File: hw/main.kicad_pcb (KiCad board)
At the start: 2 copper layers, 90 parts, among them J1 UART_01X03, J2 SWD_01X04, J3 SWD_01X04, J4 IDC_02X07, J5 IDC_02X07, J8 SMA, SW1 LCD_BTN, U1 STM32F405RGTx, U10 MCP1826S, U11 MCP1826S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

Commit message: placement component to pcb
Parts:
- removed U12: OSRB38C9BA, KLIB_Opto:OSRB8C9BA
- added C36: 100n, Capacitor_SMD:C_0805_2012Metric, F.Cu at (167.0, 100.3)
- added C37: 1u/50V, Capacitor_SMD:C_0805_2012Metric, F.Cu at (167.0, 98.4)
- added D2: LTST-G563ZEGBW, KLIB_Opto:LED_RGB_5050-6, F.Cu at (140.0, 60.0)
- added D3: LTST-G563ZEGBW, KLIB_Opto:LED_RGB_5050-6, F.Cu at (95.0, 80.0)
- added D4: LTST-G563ZEGBW, KLIB_Opto:LED_RGB_5050-6, F.Cu at (140.0, 100.0)
- added D5: LTST-G563ZEGBW, KLIB_Opto:LED_RGB_5050-6, F.Cu at (185.0, 80.0)
- added H1: M3, KLIB_Mechanical:Bolt_M3, F.Cu at (90.0, 40.0)
- added H2: M3, KLIB_Mechanical:Bolt_M3, F.Cu at (190.0, 40.0)
- added H3: M3, KLIB_Mechanical:Bolt_M3, F.Cu at (190.0, 115.0)
- added H4: M3, KLIB_Mechanical:Bolt_M3, F.Cu at (90.0, 115.0)
- added J6: IDC_02X03, Connector_IDC:IDC-Header_2x03_P2.54mm_Vertical, F.Cu at (137.5, 41.0)
- added J7: IDC_02X13, Connector_IDC:IDC-Header_2x13_P2.54mm_Vertical, F.Cu at (91.8, 51.0)
- added J9: IDC_02X05, Connector_IDC:IDC-Header_2x05_P2.54mm_Vertical, F.Cu at (91.0, 101.1)
- U11: value MCP1826S -> OSRB38C9BA; footprint Package_TO_SOT_SMD:SOT-223-3_TabPin2 -> KLIB_Opto:OSRB8C9BA_Horizontal
- U6: value AD8542 -> STM32F405RGTx; footprint Package_SO:SOIJ-8_5.3x5.3mm_P1.27mm -> Package_QFP:TQFP-64_10x10mm_P0.5mm
- U7: value STM32F405RGTx -> HM-TRP-869S; footprint Package_QFP:TQFP-64_10x10mm_P0.5mm -> KLIB_RF_Module:HM-TRP-SMD
- U8: value HM-TRP-869S -> ULN2003; footprint KLIB_RF_Module:HM-TRP-SMD -> Package_SO:SOIC-16_3.9x9.9mm_P1.27mm
- U9: value ULN2003 -> MCP1826S; footprint Package_SO:SOIC-16_3.9x9.9mm_P1.27mm -> Package_TO_SOT_SMD:SOT-223-3_TabPin2
- moved C26 121.4 mm to (92.0, 108.2), turned to 180 degrees
- moved C4 119.1 mm to (100.0, 107.2), turned to 180 degrees
- moved C6 112.9 mm to (105.8, 94.0), turned to 90 degrees
- moved SW1 109.2 mm to (96.0, 113.0), turned to 270 degrees
- moved J5 109.0 mm to (165.4, 41.0), turned to 90 degrees
- moved C29 107.7 mm to (92.2, 71.8)
- moved C28 107.6 mm to (92.2, 61.6)
- moved C8 104.1 mm to (103.2, 111.2), turned to 180 degrees
- moved C27 103.5 mm to (92.2, 59.7)
- moved J2 101.7 mm to (97.0, 95.1), turned to 180 degrees
- moved C32 100.0 mm to (103.0, 61.6)
- moved C7 99.3 mm to (118.8, 106.0)
- moved J1 95.5 mm to (125.5, 116.8), turned to 270 degrees
- moved C34 95.5 mm to (103.0, 59.7)
- moved R20 95.3 mm to (101.0, 78.0)
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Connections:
- U1 pad 10: /Address/A6 -> /Address/A1
- U1 pad 11: /Address/A7 -> /Address/A0
- U1 pad 3: /Address/A0 -> /Address/A7
- U1 pad 4: /Address/A1 -> /Address/A6
- U1 pad 5: /Address/A2 -> /Address/A5
- U1 pad 6: /Address/A3 -> /Address/A4
- U1 pad 8: /Address/A4 -> /Address/A3
- U1 pad 9: /Address/A5 -> /Address/A2
- U10 pad 1: +5V5 -> +5V
- U10 pad 3: +5V -> +3V3
- U11 pad 1: +5V -> /Back/IR_RX
- U11 pad 3: +3V3 -> Net-(C35-Pad1)
- U3 pad 5: Net-(C13-Pad1) -> Net-(C11-Pad1)
- U3 pad 6: Net-(C15-Pad2) -> Net-(C12-Pad2)
- U3 pad 7: Net-(C15-Pad2) -> Net-(C12-Pad2)
- U5 pad 1: Net-(C12-Pad2) -> Net-(C15-Pad2)
- U5 pad 2: Net-(C12-Pad2) -> Net-(C15-Pad2)
- U5 pad 3: Net-(C11-Pad1) -> Net-(C13-Pad1)
- U5 pad 5: (no net) -> Net-(C15-Pad2)
- U5 pad 6: (no net) -> Net-(C17-Pad2)
- U5 pad 7: (no net) -> Net-(C17-Pad2)
- U6 pad 1: Net-(C17-Pad2) -> +3V3
- U6 pad 2: Net-(C17-Pad2) -> Net-(U6-Pad2)
- U6 pad 3: Net-(C15-Pad2) -> Net-(U6-Pad3)
- U6 pad 4: (no net) -> Net-(U6-Pad4)
- U6 pad 5: (no net) -> Net-(U6-Pad5)
- U6 pad 6: (no net) -> Net-(U6-Pad6)
- U6 pad 7: (no net) -> /Sound/Sound MCU/~RST
- U6 pad 8: (no net) -> Net-(U6-Pad8)
- U7 pad 2: Net-(U7-Pad2) -> /Main MCU/RF_UART_RX
- U7 pad 3: Net-(U7-Pad3) -> GND
- U7 pad 4: Net-(U7-Pad4) -> /RF/RF_UART_RX
- U7 pad 5: Net-(U7-Pad5) -> /Main MCU/~RF_CONFIG
- U7 pad 6: Net-(U7-Pad6) -> /Main MCU/~RF_ENABLE
- U7 pad 7: /Sound/Sound MCU/~RST -> Net-(U7-Pad7)
- U7 pad 8: Net-(U7-Pad8) -> GND
- U7 pad 9: Net-(U7-Pad9) -> Net-(D1-Pad1)
- U8 pad 1: +3V3 -> /LED/PWM_R
- U8 pad 2: /Main MCU/RF_UART_RX -> /LED/PWM_R
- U8 pad 3: GND -> /LED/PWM_G
- U8 pad 4: /RF/RF_UART_RX -> /LED/PWM_G
- U8 pad 5: /Main MCU/~RF_CONFIG -> /LED/PWM_B
- U8 pad 6: /Main MCU/~RF_ENABLE -> /LED/PWM_B
- U8 pad 7: Net-(U8-Pad7) -> /LED/PWM_B
- U8 pad 9: Net-(D1-Pad1) -> +5V
- U9 pad 1: /LED/PWM_R -> +5V5
- U9 pad 2: /LED/PWM_R -> GND
- U9 pad 3: /LED/PWM_G -> +5V
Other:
- board outline added: 110 x 85 mm

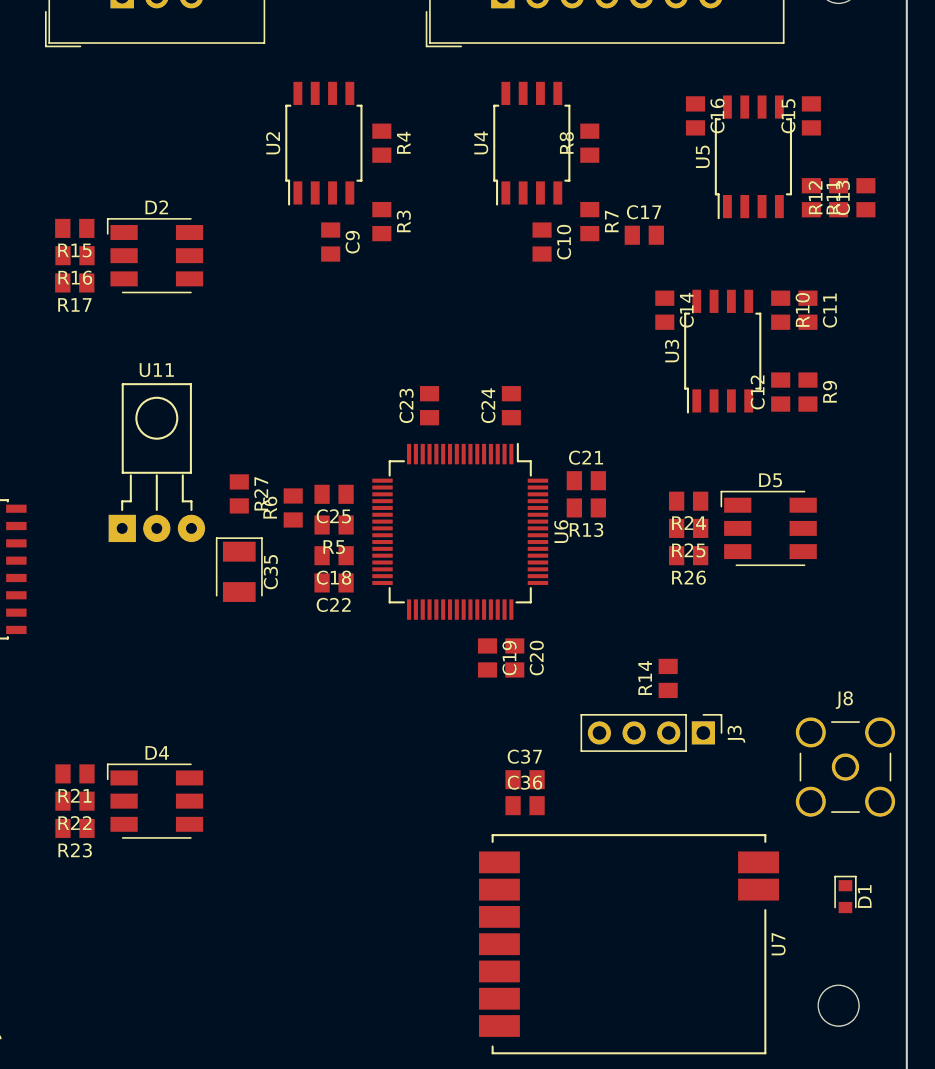
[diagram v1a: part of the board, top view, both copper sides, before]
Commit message: updated schematic added buffer to gun uart and updated pcb
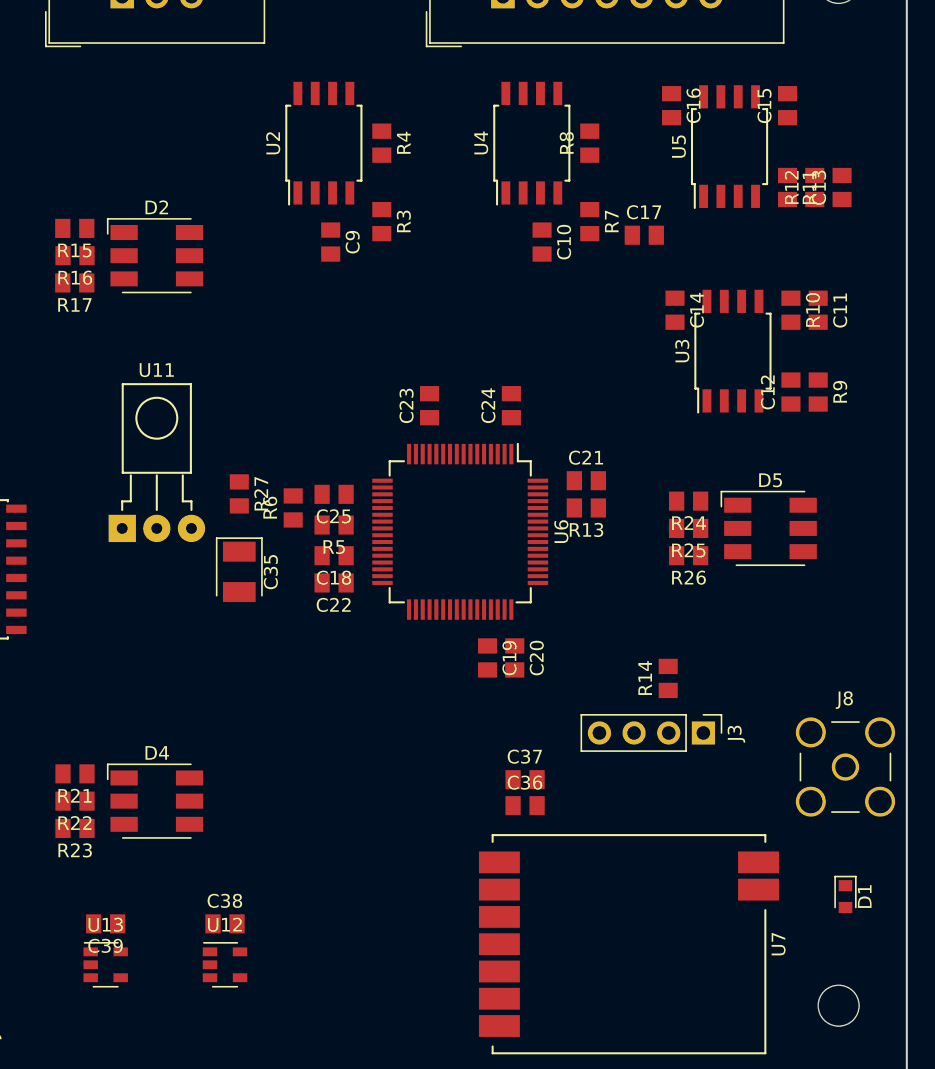
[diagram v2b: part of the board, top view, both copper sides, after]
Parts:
- added C38: 100n, Capacitor_SMD:C_0805_2012Metric, F.Cu at (145.0, 109.0)
- added C39: 100n, Capacitor_SMD:C_0805_2012Metric, F.Cu at (136.2, 109.0)
- added U12: 74AHC1G08, Package_TO_SOT_SMD:SOT-23-5, F.Cu at (145.0, 112.0)
- added U13: 74AHC1G08, Package_TO_SOT_SMD:SOT-23-5, F.Cu at (136.2, 112.0)
- moved C13 1.90 mm to (190.2, 55.0)
- moved C15 1.90 mm to (186.2, 49.0)
- moved C16 1.90 mm to (177.8, 49.0)
- moved R11 1.90 mm to (186.2, 55.0)
- moved R12 1.90 mm to (188.2, 55.0)
- moved U5 1.90 mm to (182.0, 52.0)
- moved C11 0.75 mm to (188.5, 64.0)
- moved C12 0.75 mm to (186.5, 70.0)
- moved C14 0.75 mm to (178.0, 64.0)
- moved R10 0.75 mm to (186.5, 64.0)
- moved R9 0.75 mm to (188.5, 70.0)
- moved U3 0.75 mm to (182.2, 67.0)
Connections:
- J9 pad 5: /Gun/GUN_UART_RX -> /Gun/GUN_RX
- J9 pad 6: /Gun/GUN_UART_RX -> /Gun/GUN_RX
- J9 pad 7: /Main MCU/GUN_UART_RX -> /Gun/GUN_TX
- J9 pad 8: /Main MCU/GUN_UART_RX -> /Gun/GUN_TX

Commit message: updated pcb placement
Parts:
- moved J7 12.3 mm to (99.0, 41.0)
- moved J4 10.0 mm to (99.0, 51.0)
- moved J6 7.54 mm to (145.0, 41.0)
- moved U8 6.00 mm to (121.0, 83.0), turned to 90 degrees
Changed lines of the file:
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@@
   )
   (module Connector_IDC:IDC-Header_2x03_P2.54mm_Vertical (layer F.Cu)
-    (at 137.46 41 90)
+    (at 145 41 90)
     (descr "Through hole straight IDC box header, 2x03, 2.54mm pitch, double rows")
     (tags "Through hole IDC box header THT 2x03 2.54mm double row")
@@
   )
   (module Connector_IDC:IDC-Header_2x07_P2.54mm_Vertical (layer F.Cu)
-    (at 99.38 41 90)
+    (at 99 51 90)
     (descr "Through hole straight IDC box header, 2x07, 2.54mm pitch, double rows")
     (tags "Through hole IDC box header THT 2x07 2.54mm double row")
@@
   )
   (module Connector_IDC:IDC-Header_2x13_P2.54mm_Vertical (layer F.Cu)
-    (at 91.76 51 90)
+    (at 99 41 90)
     (descr "Through hole straight IDC box header, 2x13, 2.54mm pitch, double rows")
     (tags "Through hole IDC box header THT 2x13 2.54mm double row")
@@
   )
   (module Package_SO:SOIC-16_3.9x9.9mm_P1.27mm (layer F.Cu)
-    (at 127 83)
+    (at 121 83 90)
     (descr "16-Lead Plastic Small Outline (SL) - Narrow, 3.90 mm Body [SOIC] (see Microchip Packaging Specification 00000049BS.pdf)")
     (tags "SOIC 1.27")
     (attr smd)
-    (fp_text reference U8 (at 0 -6) (layer F.SilkS)
-      (effects (font (size 1 1) (thickness 0.15)))
-    )
-    (fp_text value ULN2003 (at 0 6) (layer F.Fab)
-      (effects (font (size 1 1) (thickness 0.15)))
-    )
-    (fp_text user %R (at 0 0) (layer F.Fab)
+    (fp_text reference U8 (at 0 -6 90) (layer F.SilkS)
+      (effects (font (size 1 1) (thickness 0.15)))
+    )
+    (fp_text value ULN2003 (at 0 6 90) (layer F.Fab)
+      (effects (font (size 1 1) (thickness 0.15)))
+    )
+    (fp_text user %R (at 0 0 90) (layer F.Fab)
       (effects (font (size 0.9 0.9) (thickness 0.135)))
     )
@@
     (fp_line (start -2.075 5.075) (end 2.075 5.075) (layer F.SilkS) (width 0.15))
     (fp_line (start -2.075 -5.05) (end -3.45 -5.05) (layer F.SilkS) (width 0.15))
-    (pad 1 smd rect (at -2.7 -4.445) (size 1.5 0.6) (layers F.Cu F.Paste F.Mask)
+    (pad 1 smd rect (at -2.7 -4.445 90) (size 1.5 0.6) (layers F.Cu F.Paste F.Mask)
       (net 53 /LED/PWM_R))
-    (pad 2 smd rect (at -2.7 -3.175) (size 1.5 0.6) (layers F.Cu F.Paste F.Mask)
+    (pad 2 smd rect (at -2.7 -3.175 90) (size 1.5 0.6) (layers F.Cu F.Paste F.Mask)
       (net 53 /LED/PWM_R))
-    (pad 3 smd rect (at -2.7 -1.905) (size 1.5 0.6) (layers F.Cu F.Paste F.Mask)
+    (pad 3 smd rect (at -2.7 -1.905 90) (size 1.5 0.6) (layers F.Cu F.Paste F.Mask)
       (net 54 /LED/PWM_G))
-    (pad 4 smd rect (at -2.7 -0.635) (size 1.5 0.6) (layers F.Cu F.Paste F.Mask)
+    (pad 4 smd rect (at -2.7 -0.635 90) (size 1.5 0.6) (layers F.Cu F.Paste F.Mask)
       (net 54 /LED/PWM_G))
-    (pad 5 smd rect (at -2.7 0.635) (size 1.5 0.6) (layers F.Cu F.Paste F.Mask)
+    (pad 5 smd rect (at -2.7 0.635 90) (size 1.5 0.6) (layers F.Cu F.Paste F.Mask)
       (net 55 /LED/PWM_B))
-    (pad 6 smd rect (at -2.7 1.905) (size 1.5 0.6) (layers F.Cu F.Paste F.Mask)
+    (pad 6 smd rect (at -2.7 1.905 90) (size 1.5 0.6) (layers F.Cu F.Paste F.Mask)
       (net 55 /LED/PWM_B))
-    (pad 7 smd rect (at -2.7 3.175) (size 1.5 0.6) (layers F.Cu F.Paste F.Mask)
+    (pad 7 smd rect (at -2.7 3.175 90) (size 1.5 0.6) (layers F.Cu F.Paste F.Mask)
       (net 55 /LED/PWM_B))
-    (pad 8 smd rect (at -2.7 4.445) (size 1.5 0.6) (layers F.Cu F.Paste F.Mask)
-      (net 2 GND))
-    (pad 9 smd rect (at 2.7 4.445) (size 1.5 0.6) (layers F.Cu F.Paste F.Mask)
-      (net 13 +5V))
-    (pad 10 smd rect (at 2.7 3.175) (size 1.5 0.6) (layers F.Cu F.Paste F.Mask)
+    (pad 8 smd rect (at -2.7 4.445 90) (size 1.5 0.6) (layers F.Cu F.Paste F.Mask)
+      (net 2 GND))
+    (pad 9 smd rect (at 2.7 4.445 90) (size 1.5 0.6) (layers F.Cu F.Paste F.Mask)
+      (net 13 +5V))
+    (pad 10 smd rect (at 2.7 3.175 90) (size 1.5 0.6) (layers F.Cu F.Paste F.Mask)
       (net 15 /Back/LED_PWM_B))
-    (pad 11 smd rect (at 2.7 1.905) (size 1.5 0.6) (layers F.Cu F.Paste F.Mask)
+    (pad 11 smd rect (at 2.7 1.905 90) (size 1.5 0.6) (layers F.Cu F.Paste F.Mask)
       (net 15 /Back/LED_PWM_B))
-    (pad 12 smd rect (at 2.7 0.635) (size 1.5 0.6) (layers F.Cu F.Paste F.Mask)
+    (pad 12 smd rect (at 2.7 0.635 90) (size 1.5 0.6) (layers F.Cu F.Paste F.Mask)
       (net 15 /Back/LED_PWM_B))
-    (pad 13 smd rect (at 2.7 -0.635) (size 1.5 0.6) (layers F.Cu F.Paste F.Mask)
+    (pad 13 smd rect (at 2.7 -0.635 90) (size 1.5 0.6) (layers F.Cu F.Paste F.Mask)
       (net 24 /Back/LED_PWM_G))
-    (pad 14 smd rect (at 2.7 -1.905) (size 1.5 0.6) (layers F.Cu F.Paste F.Mask)
+    (pad 14 smd rect (at 2.7 -1.905 90) (size 1.5 0.6) (layers F.Cu F.Paste F.Mask)
       (net 24 /Back/LED_PWM_G))
-    (pad 15 smd rect (at 2.7 -3.175) (size 1.5 0.6) (layers F.Cu F.Paste F.Mask)
+    (pad 15 smd rect (at 2.7 -3.175 90) (size 1.5 0.6) (layers F.Cu F.Paste F.Mask)
       (net 11 /Back/LED_PWM_R))
-    (pad 16 smd rect (at 2.7 -4.445) (size 1.5 0.6) (layers F.Cu F.Paste F.Mask)
+    (pad 16 smd rect (at 2.7 -4.445 90) (size 1.5 0.6) (layers F.Cu F.Paste F.Mask)
       (net 11 /Back/LED_PWM_R))
     (model ${KISYS3DMOD}/Package_SO.3dshapes/SOIC-16_3.9x9.9mm_P1.27mm.wrl

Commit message: updated pcb
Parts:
- moved C38 12.1 mm to (133.0, 107.2)
- moved U12 12.1 mm to (133.0, 110.2), turned to 90 degrees
- moved C39 9.66 mm to (126.8, 107.2), turned to 0 degrees
- moved U13 9.66 mm to (126.8, 110.2), turned to 90 degrees
- moved C26 8.46 mm to (99.0, 113.0), turned to 270 degrees
- moved R6 4.24 mm to (153.0, 75.5), turned to 0 degrees
- moved C19 4.03 mm to (168.2, 90.0), turned to 0 degrees
- moved C20 2.50 mm to (168.2, 88.0), turned to 0 degrees
- moved D1 1.80 mm to (191.5, 105.5), turned to 315 degrees
- moved C5 0.50 mm to (113.9, 112.0)
- moved U7 0.38 mm to (174.2, 110.5)
- moved R5 0.25 mm to (153.0, 79.5)
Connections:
- U1 pad 22: /LED/PWM_R -> /LED/PWM_B
- U1 pad 26: /LED/PWM_B -> /LED/PWM_R
- U6 pad 14: /Main MCU/SOUND_SEL0 -> Net-(U6-Pad14)
- U6 pad 15: /Main MCU/SOUND_SEL1 -> Net-(U6-Pad15)
- U6 pad 44: Net-(U6-Pad44) -> /Main MCU/SOUND_SEL0
- U6 pad 45: Net-(U6-Pad45) -> /Main MCU/SOUND_SEL1
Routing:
- net /Main MCU/SOUND_SEL1: track 0.00 -> 62.5 mm, vias 0 -> 2
- net /Main MCU/SOUND_SEL0: track 0.00 -> 61.7 mm, vias 0 -> 2
- net /Sound/SOUND_UART_RX: track 0.00 -> 60.8 mm, vias 0 -> 2
- net /Main MCU/SOUND_UART_RX: track 0.00 -> 60.3 mm, vias 0 -> 2
- net +3V3: track 0.00 -> 35.8 mm
- net /LED/PWM_R: track 0.00 -> 29.6 mm
- net /LED/PWM_B: track 0.00 -> 28.6 mm
- net /LED/PWM_G: track 0.00 -> 28.5 mm
- net /Main MCU/SWDIO: track 0.00 -> 23.3 mm
- net /Gun/GUN_UART_RX: track 0.00 -> 23.1 mm
- net /Main MCU/GUN_UART_RX: track 0.00 -> 22.2 mm
- net +5V5: track 0.00 -> 17.8 mm
- net /Main MCU/SWDCLK: track 0.00 -> 17.7 mm
- net /Display/~BTN: track 0.00 -> 16.9 mm
- net /Main MCU/DEBUG_UART_RX: track 0.00 -> 15.0 mm
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- added copper zone on B.Cu, net GND
- added copper zone on F.Cu, net GND

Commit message: updated pcb
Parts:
- moved C2 4.28 mm to (103.5, 93.5), turned to 180 degrees
- moved C6 2.70 mm to (103.5, 95.5), turned to 180 degrees
- moved R2 2.30 mm to (99.8, 90.8), turned to 270 degrees
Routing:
- net /Main MCU/~RF_CONFIG: track 0.00 -> 73.5 mm, vias 0 -> 2
- net /Main MCU/~RF_ENABLE: track 0.00 -> 71.0 mm, vias 0 -> 2
- net /Main MCU/RF_UART_RX: track 0.00 -> 69.2 mm, vias 0 -> 2
- net /RF/RF_UART_RX: track 0.00 -> 65.5 mm, vias 0 -> 2
- net /Main MCU/SWDIO: track 23.3 -> 16.9 mm
- net Net-(C2-Pad1): track 3.77 -> 5.33 mm

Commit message: updated pcb
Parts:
- moved C34 19.6 mm to (122.0, 64.8), turned to 90 degrees
- moved C33 18.4 mm to (120.0, 64.8), turned to 90 degrees
- moved C30 14.8 mm to (104.0, 64.8), turned to 90 degrees
- moved U10 12.1 mm to (115.2, 64.8), turned to 90 degrees
- moved C29 12.0 mm to (102.0, 64.8), turned to 90 degrees
- moved C31 10.5 mm to (108.5, 64.8), turned to 90 degrees
- moved C32 8.11 mm to (110.5, 64.8), turned to 90 degrees
- moved U9 5.37 mm to (97.2, 64.8), turned to 90 degrees
- moved C27 5.35 mm to (90.5, 64.8), turned to 90 degrees
- moved C28 3.17 mm to (92.5, 64.8), turned to 90 degrees
- moved R14 2.00 mm to (177.5, 89.0), turned to 270 degrees
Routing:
- net +5V5: track 17.8 -> 110.9 mm
- net /Sound/Sound MCU/~RST: track 0.00 -> 37.1 mm, vias 0 -> 1
- net +5V: track 10.2 -> 32.7 mm
- net /Sound/Sound MCU/SWDCLK: track 0.00 -> 15.4 mm
- net /Sound/Sound MCU/SWDIO: track 0.00 -> 14.5 mm
- net +3V3: track 36.3 -> 44.7 mm
- net /Main MCU/~RF_CONFIG: track 73.5 -> 72.4 mm
